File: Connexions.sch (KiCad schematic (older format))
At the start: 7 parts, among them J10 Sense2, J11 I2C, J12 Serial, J13 I2S, J7 PWM, J8 IO, J9 Sense1

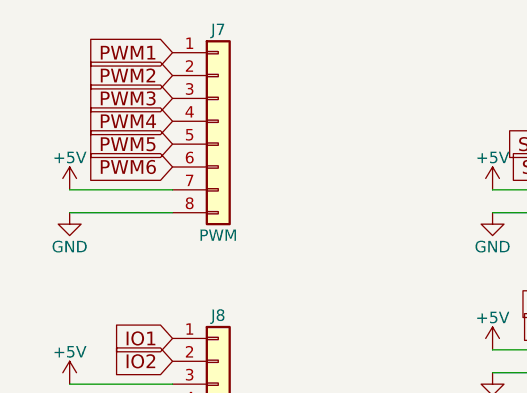
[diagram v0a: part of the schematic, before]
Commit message: Board should be ok. Bargraph leds yet to do.
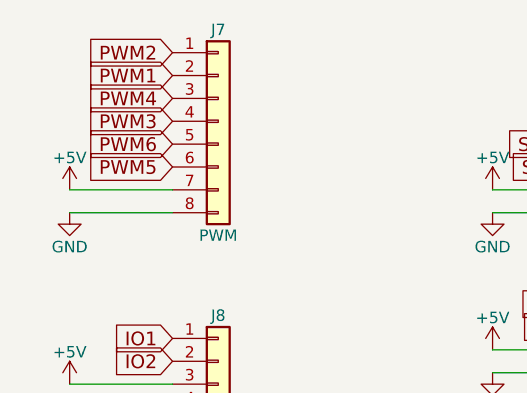
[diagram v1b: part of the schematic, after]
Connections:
- net PWM1: now also J7.2 (Pin_2); no longer J7.1 (Pin_1)
- net PWM2: now also J7.1 (Pin_1); no longer J7.2 (Pin_2)
- net PWM3: now also J7.4 (Pin_4); no longer J7.3 (Pin_3)
- net PWM4: now also J7.3 (Pin_3); no longer J7.4 (Pin_4)
- net PWM5: now also J7.6 (Pin_6); no longer J7.5 (Pin_5)
- net PWM6: now also J7.5 (Pin_5); no longer J7.6 (Pin_6)
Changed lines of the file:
@@
 Text GLabel 5700 3900 0    60   Input ~ 0
 IO2
+Text GLabel 5700 2650 0    60   Input ~ 0
+PWM1
 Text GLabel 5700 2550 0    60   Input ~ 0
-PWM1
-Text GLabel 5700 2650 0    60   Input ~ 0
 PWM2
+Text GLabel 5700 2850 0    60   Input ~ 0
+PWM3
 Text GLabel 5700 2750 0    60   Input ~ 0
-PWM3
-Text GLabel 5700 2850 0    60   Input ~ 0
 PWM4
+Text GLabel 5700 3050 0    60   Input ~ 0
+PWM5
 Text GLabel 5700 2950 0    60   Input ~ 0
-PWM5
-Text GLabel 5700 3050 0    60   Input ~ 0
 PWM6
 $Comp

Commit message: Seems to be good for fabrication launch. Probably minor things to fix.
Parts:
- renumbered J8 to J10, J9 to J11, J10 to J12, J11 to J13, J12 to J14, J13 to J15, J7 to J9
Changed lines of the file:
@@
 PWM6
 $Comp
-L Audio-Jack-2 J9
+L Audio-Jack-2 J11
 U 1 1 59B10A38
 P 5900 4500
-F 0 "J9" H 5875 4575 50  0000 C CNN
+F 0 "J11" H 5875 4575 50  0000 C CNN
 F 1 "Sense1" H 5875 4325 50  0000 C CNN
 F 2 "Connectors:PJ320D_3.5mm_Jack" H 6150 4500 50  0001 C CNN
@@
 $EndComp
 $Comp
-L GND #PWR076
+L GND #PWR080
 U 1 1 59B10AB7
 P 5600 4700
-F 0 "#PWR076" H 5600 4450 50  0001 C CNN
+F 0 "#PWR080" H 5600 4450 50  0001 C CNN
 F 1 "GND" H 5600 4550 50  0000 C CNN
 F 2 "" H 5600 4700 50  0001 C CNN
@@
 	5600 4500 5700 4500
 $Comp
-L Audio-Jack-2 J10
+L Audio-Jack-2 J12
 U 1 1 59B10F7B
 P 5900 5250
-F 0 "J10" H 5875 5325 50  0000 C CNN
+F 0 "J12" H 5875 5325 50  0000 C CNN
 F 1 "Sense2" H 5875 5075 50  0000 C CNN
 F 2 "Connectors:PJ320D_3.5mm_Jack" H 6150 5250 50  0001 C CNN
@@
 $EndComp
 $Comp
-L GND #PWR077
+L GND #PWR081
 U 1 1 59B10F81
 P 5600 5450
-F 0 "#PWR077" H 5600 5200 50  0001 C CNN
+F 0 "#PWR081" H 5600 5200 50  0001 C CNN
 F 1 "GND" H 5600 5300 50  0000 C CNN
 F 2 "" H 5600 5450 50  0001 C CNN
@@
 	5600 5250 5700 5250
 $Comp
-L Conn_01x04 J11
+L Conn_01x04 J13
 U 1 1 59B12058
 P 7650 3050
-F 0 "J11" H 7650 3250 50  0000 C CNN
+F 0 "J13" H 7650 3250 50  0000 C CNN
 F 1 "I2C" H 7650 2750 50  0000 C CNN
 F 2 "Pin_Headers:Pin_Header_Straight_1x04_Pitch2.54mm" H 7650 3050 50  0001 C CNN
@@
 I2S_MCK
 $Comp
-L Conn_01x08 J7
+L Conn_01x08 J9
 U 1 1 59B1CBF4
 P 5900 2850
-F 0 "J7" H 5900 3250 50  0000 C CNN
+F 0 "J9" H 5900 3250 50  0000 C CNN
 F 1 "PWM" H 5900 2350 50  0000 C CNN
 F 2 "Pin_Headers:Pin_Header_Straight_1x08_Pitch2.54mm" H 5900 2850 50  0001 C CNN
@@
 $EndComp
 $Comp
-L +5V #PWR078
+L +5V #PWR082
 U 1 1 59B1CCA8
 P 5250 3150
-F 0 "#PWR078" H 5250 3000 50  0001 C CNN
+F 0 "#PWR082" H 5250 3000 50  0001 C CNN
 F 1 "+5V" H 5250 3290 50  0000 C CNN
 F 2 "" H 5250 3150 50  0001 C CNN
@@
 	5250 3150 5700 3150
 $Comp
-L GND #PWR079
+L GND #PWR083
 U 1 1 59B1CCEC
 P 5250 3250
-F 0 "#PWR079" H 5250 3000 50  0001 C CNN
+F 0 "#PWR083" H 5250 3000 50  0001 C CNN
 F 1 "GND" H 5250 3100 50  0000 C CNN
 F 2 "" H 5250 3250 50  0001 C CNN
@@
 	5250 3250 5700 3250
 $Comp
-L Conn_01x04 J8
+L Conn_01x04 J10
 U 1 1 59B1CDBB
 P 5900 3900
-F 0 "J8" H 5900 4100 50  0000 C CNN
+F 0 "J10" H 5900 4100 50  0000 C CNN
 F 1 "IO" H 5900 3600 50  0000 C CNN
 F 2 "Pin_Headers:Pin_Header_Straight_1x04_Pitch2.54mm" H 5900 3900 50  0001 C CNN
@@
 $EndComp
 $Comp
-L +5V #PWR080
+L +5V #PWR084
 U 1 1 59B1CE5C
 P 5250 4000
-F 0 "#PWR080" H 5250 3850 50  0001 C CNN
+F 0 "#PWR084" H 5250 3850 50  0001 C CNN
 F 1 "+5V" H 5250 4140 50  0000 C CNN
 F 2 "" H 5250 4000 50  0001 C CNN
@@
 $EndComp
 $Comp
-L GND #PWR081
+L GND #PWR085
 U 1 1 59B1CE7C
 P 5250 4100
-F 0 "#PWR081" H 5250 3850 50  0001 C CNN
+F 0 "#PWR085" H 5250 3850 50  0001 C CNN
 F 1 "GND" H 5250 3950 50  0000 C CNN
 F 2 "" H 5250 4100 50  0001 C CNN
@@
 	5700 4000 5250 4000
 $Comp
-L Conn_01x04 J12
+L Conn_01x04 J14
 U 1 1 59B1D305
 P 7650 3750
-F 0 "J12" H 7650 3950 50  0000 C CNN
+F 0 "J14" H 7650 3950 50  0000 C CNN
 F 1 "Serial" H 7650 3450 50  0000 C CNN
 F 2 "Pin_Headers:Pin_Header_Straight_1x04_Pitch2.54mm" H 7650 3750 50  0001 C CNN
@@
 TX
 $Comp
-L +5V #PWR082
+L +5V #PWR086
 U 1 1 59B1D44B
 P 7100 3150
-F 0 "#PWR082" H 7100 3000 50  0001 C CNN
+F 0 "#PWR086" H 7100 3000 50  0001 C CNN
 F 1 "+5V" H 7100 3290 50  0000 C CNN
 F 2 "" H 7100 3150 50  0001 C CNN
@@
 $EndComp
 $Comp
-L GND #PWR083
+L GND #PWR087
 U 1 1 59B1D46E
 P 7100 3250
-F 0 "#PWR083" H 7100 3000 50  0001 C CNN
+F 0 "#PWR087" H 7100 3000 50  0001 C CNN
 F 1 "GND" H 7100 3100 50  0000 C CNN
 F 2 "" H 7100 3250 50  0001 C CNN
@@
 	7100 3250 7450 3250
 $Comp
-L +5V #PWR084
+L +5V #PWR088
 U 1 1 59B1D4D2
 P 7100 3850
-F 0 "#PWR084" H 7100 3700 50  0001 C CNN
+F 0 "#PWR088" H 7100 3700 50  0001 C CNN
 F 1 "+5V" H 7100 3990 50  0000 C CNN
 F 2 "" H 7100 3850 50  0001 C CNN
@@
 $EndComp
 $Comp
-L GND #PWR085
+L GND #PWR089
 U 1 1 59B1D4F5
 P 6750 4950
-F 0 "#PWR085" H 6750 4700 50  0001 C CNN
+F 0 "#PWR089" H 6750 4700 50  0001 C CNN
 F 1 "GND" H 6750 4800 50  0000 C CNN
 F 2 "" H 6750 4950 50  0001 C CNN
@@
 	7100 3950 7450 3950
 $Comp
-L Conn_01x06 J13
+L Conn_01x06 J15
 U 1 1 59B1D5B9
 P 7650 4650
-F 0 "J13" H 7650 4950 50  0000 C CNN
+F 0 "J15" H 7650 4950 50  0000 C CNN
 F 1 "I2S" H 7650 4250 50  0000 C CNN
 F 2 "Pin_Headers:Pin_Header_Straight_1x06_Pitch2.54mm" H 7650 4650 50  0001 C CNN
@@
 $EndComp
 $Comp
-L +3.3V #PWR086
+L +3.3V #PWR090
 U 1 1 59B1D6B1
 P 6750 4850
-F 0 "#PWR086" H 6750 4700 50  0001 C CNN
+F 0 "#PWR090" H 6750 4700 50  0001 C CNN
 F 1 "+3.3V" H 6750 4990 50  0000 C CNN
 F 2 "" H 6750 4850 50  0001 C CNN
@@
 	6750 4950 7450 4950
 $Comp
-L GND #PWR087
+L GND #PWR091
 U 1 1 59C9F2EB
 P 7100 3950
-F 0 "#PWR087" H 7100 3700 50  0001 C CNN
+F 0 "#PWR091" H 7100 3700 50  0001 C CNN
 F 1 "GND" H 7100 3800 50  0000 C CNN
 F 2 "" H 7100 3950 50  0001 C CNN

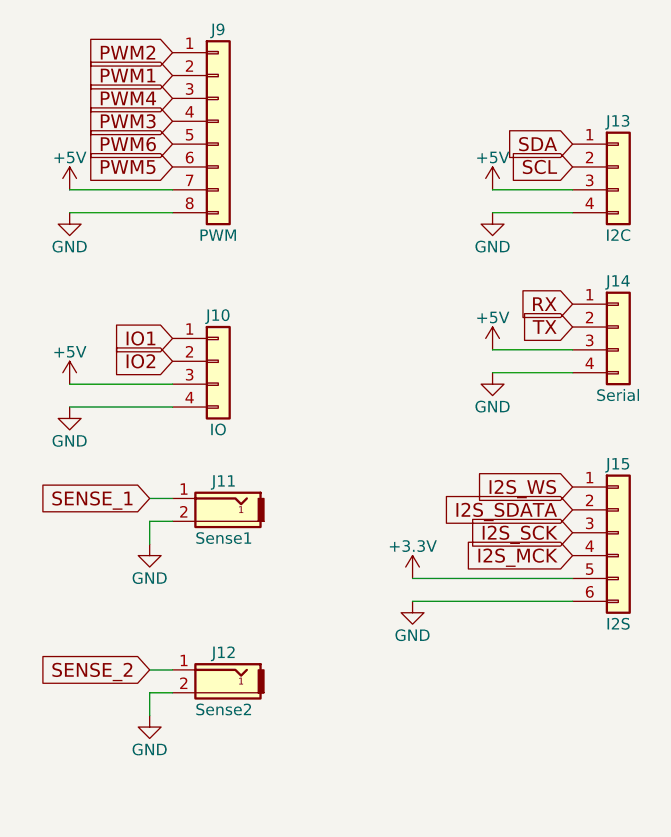
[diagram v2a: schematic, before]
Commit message: Board modified after ckecking. Ready for fab, just need to create gerber, position and components files.
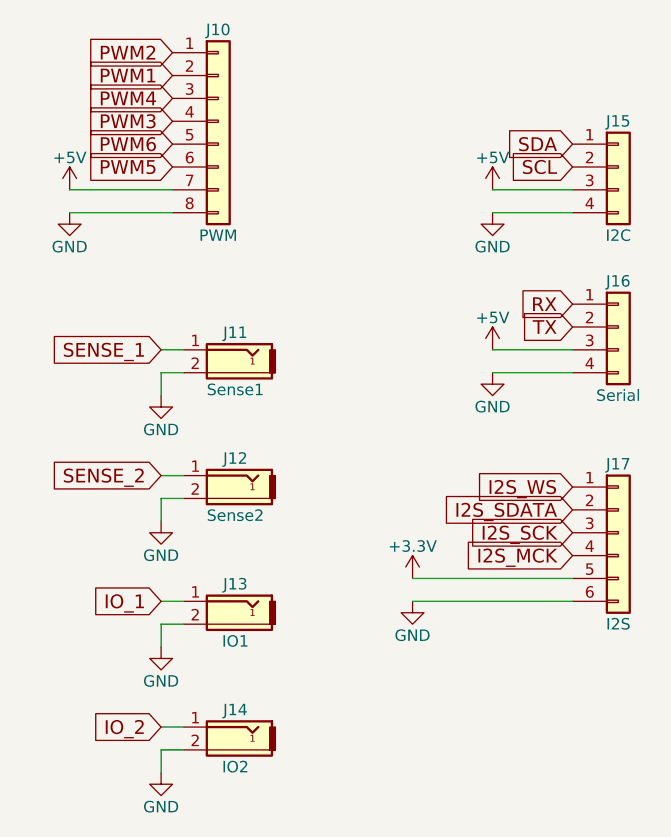
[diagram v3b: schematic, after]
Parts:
- removed J10: IO, Pin_Headers:Pin_Header_Straight_1x04_Pitch2.54mm, symbol Conn_01x04
- added J13: IO1, Connectors:PJ320D_3.5mm_Jack, symbol Audio-Jack-2
- added J14: IO2, Connectors:PJ320D_3.5mm_Jack, symbol Audio-Jack-2
- renumbered J9 to J10, J13 to J15, J14 to J16, J15 to J17
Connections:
- net GND: now also J13.2, J14.2
- new net IO_1: J13.1
- new net IO_2: J14.1
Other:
- moved on the sheet: J11, J12
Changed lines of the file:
@@
 EESchema Schematic File Version 2
+LIBS:ContactConsequencesMono-rescue
 LIBS:switches-perso
 LIBS:Logos
@@
 Comment4 ""
 $EndDescr
-Text GLabel 5700 3800 0    60   Input ~ 0
-IO1
-Text GLabel 5700 3900 0    60   Input ~ 0
-IO2
 Text GLabel 5700 2650 0    60   Input ~ 0
 PWM1
@@
 L Audio-Jack-2 J11
 U 1 1 59B10A38
-P 5900 4500
-F 0 "J11" H 5875 4575 50  0000 C CNN
-F 1 "Sense1" H 5875 4325 50  0000 C CNN
-F 2 "Connectors:PJ320D_3.5mm_Jack" H 6150 4500 50  0001 C CNN
-F 3 "" H 6150 4500 50  0001 C CNN
-	1    5900 4500
+P 5950 3850
+F 0 "J11" H 5925 3925 50  0000 C CNN
+F 1 "Sense1" H 5925 3675 50  0000 C CNN
+F 2 "Connectors:PJ320D_3.5mm_Jack" H 6200 3850 50  0001 C CNN
+F 3 "" H 6200 3850 50  0001 C CNN
+	1    5950 3850
 	-1   0    0    -1
 $EndComp
 $Comp
-L GND #PWR080
+L GND #PWR088
 U 1 1 59B10AB7
-P 5600 4700
-F 0 "#PWR080" H 5600 4450 50  0001 C CNN
-F 1 "GND" H 5600 4550 50  0000 C CNN
-F 2 "" H 5600 4700 50  0001 C CNN
-F 3 "" H 5600 4700 50  0001 C CNN
-	1    5600 4700
-	1    0    0    -1
-$EndComp
-Wire Wire Line
-	5600 4700 5600 4600
-Wire Wire Line
-	5600 4600 5700 4600
-Text GLabel 5600 4500 0    60   Input ~ 0
+P 5650 4050
+F 0 "#PWR088" H 5650 3800 50  0001 C CNN
+F 1 "GND" H 5650 3900 50  0000 C CNN
+F 2 "" H 5650 4050 50  0001 C CNN
+F 3 "" H 5650 4050 50  0001 C CNN
+	1    5650 4050
+	1    0    0    -1
+$EndComp
+Wire Wire Line
+	5650 4050 5650 3950
+Wire Wire Line
+	5650 3950 5750 3950
+Text GLabel 5650 3850 0    60   Input ~ 0
 SENSE_1
 Wire Wire Line
-	5600 4500 5700 4500
+	5650 3850 5750 3850
 $Comp
 L Audio-Jack-2 J12
 U 1 1 59B10F7B
-P 5900 5250
-F 0 "J12" H 5875 5325 50  0000 C CNN
-F 1 "Sense2" H 5875 5075 50  0000 C CNN
-F 2 "Connectors:PJ320D_3.5mm_Jack" H 6150 5250 50  0001 C CNN
-F 3 "" H 6150 5250 50  0001 C CNN
-	1    5900 5250
+P 5950 4400
+F 0 "J12" H 5925 4475 50  0000 C CNN
+F 1 "Sense2" H 5925 4225 50  0000 C CNN
+F 2 "Connectors:PJ320D_3.5mm_Jack" H 6200 4400 50  0001 C CNN
+F 3 "" H 6200 4400 50  0001 C CNN
+	1    5950 4400
 	-1   0    0    -1
 $EndComp
 $Comp
-L GND #PWR081
+L GND #PWR089
 U 1 1 59B10F81
-P 5600 5450
-F 0 "#PWR081" H 5600 5200 50  0001 C CNN
-F 1 "GND" H 5600 5300 50  0000 C CNN
-F 2 "" H 5600 5450 50  0001 C CNN
-F 3 "" H 5600 5450 50  0001 C CNN
-	1    5600 5450
-	1    0    0    -1
-$EndComp
-Wire Wire Line
-	5600 5450 5600 5350
-Wire Wire Line
-	5600 5350 5700 5350
-Text GLabel 5600 5250 0    60   Input ~ 0
+P 5650 4600
+F 0 "#PWR089" H 5650 4350 50  0001 C CNN
+F 1 "GND" H 5650 4450 50  0000 C CNN
+F 2 "" H 5650 4600 50  0001 C CNN
+F 3 "" H 5650 4600 50  0001 C CNN
+	1    5650 4600
+	1    0    0    -1
+$EndComp
+Wire Wire Line
+	5650 4600 5650 4500
+Wire Wire Line
+	5650 4500 5750 4500
+Text GLabel 5650 4400 0    60   Input ~ 0
 SENSE_2
 Wire Wire Line
-	5600 5250 5700 5250
-$Comp
-L Conn_01x04 J13
+	5650 4400 5750 4400
+$Comp
+L Conn_01x04 J15
 U 1 1 59B12058
 P 7650 3050
-F 0 "J13" H 7650 3250 50  0000 C CNN
+F 0 "J15" H 7650 3250 50  0000 C CNN
 F 1 "I2C" H 7650 2750 50  0000 C CNN
 F 2 "Pin_Headers:Pin_Header_Straight_1x04_Pitch2.54mm" H 7650 3050 50  0001 C CNN
@@
 I2S_MCK
 $Comp
-L Conn_01x08 J9
+L Conn_01x08 J10
 U 1 1 59B1CBF4
 P 5900 2850
-F 0 "J9" H 5900 3250 50  0000 C CNN
+F 0 "J10" H 5900 3250 50  0000 C CNN
 F 1 "PWM" H 5900 2350 50  0000 C CNN
 F 2 "Pin_Headers:Pin_Header_Straight_1x08_Pitch2.54mm" H 5900 2850 50  0001 C CNN
@@
 $EndComp
 $Comp
-L +5V #PWR082
+L +5V #PWR090
 U 1 1 59B1CCA8
 P 5250 3150
-F 0 "#PWR082" H 5250 3000 50  0001 C CNN
+F 0 "#PWR090" H 5250 3000 50  0001 C CNN
 F 1 "+5V" H 5250 3290 50  0000 C CNN
 F 2 "" H 5250 3150 50  0001 C CNN
@@
 	5250 3150 5700 3150
 $Comp
-L GND #PWR083
+L GND #PWR091
 U 1 1 59B1CCEC
 P 5250 3250
-F 0 "#PWR083" H 5250 3000 50  0001 C CNN
+F 0 "#PWR091" H 5250 3000 50  0001 C CNN
 F 1 "GND" H 5250 3100 50  0000 C CNN
 F 2 "" H 5250 3250 50  0001 C CNN
@@
 	5250 3250 5700 3250
 $Comp
-L Conn_01x04 J10
-U 1 1 59B1CDBB
-P 5900 3900
-F 0 "J10" H 5900 4100 50  0000 C CNN
-F 1 "IO" H 5900 3600 50  0000 C CNN
-F 2 "Pin_Headers:Pin_Header_Straight_1x04_Pitch2.54mm" H 5900 3900 50  0001 C CNN
-F 3 "" H 5900 3900 50  0001 C CNN
-	1    5900 3900
-	1    0    0    -1
-$EndComp
-$Comp
-L +5V #PWR084
-U 1 1 59B1CE5C
-P 5250 4000
-F 0 "#PWR084" H 5250 3850 50  0001 C CNN
-F 1 "+5V" H 5250 4140 50  0000 C CNN
-F 2 "" H 5250 4000 50  0001 C CNN
-F 3 "" H 5250 4000 50  0001 C CNN
-	1    5250 4000
-	1    0    0    -1
-$EndComp
-$Comp
-L GND #PWR085
-U 1 1 59B1CE7C
-P 5250 4100
-F 0 "#PWR085" H 5250 3850 50  0001 C CNN
-F 1 "GND" H 5250 3950 50  0000 C CNN
-F 2 "" H 5250 4100 50  0001 C CNN
-F 3 "" H 5250 4100 50  0001 C CNN
-	1    5250 4100
-	1    0    0    -1
-$EndComp
-Wire Wire Line
-	5250 4100 5700 4100
-Wire Wire Line
-	5700 4000 5250 4000
-$Comp
-L Conn_01x04 J14
+L Conn_01x04 J16
 U 1 1 59B1D305
 P 7650 3750
-F 0 "J14" H 7650 3950 50  0000 C CNN
+F 0 "J16" H 7650 3950 50  0000 C CNN
 F 1 "Serial" H 7650 3450 50  0000 C CNN
 F 2 "Pin_Headers:Pin_Header_Straight_1x04_Pitch2.54mm" H 7650 3750 50  0001 C CNN
@@
 TX
 $Comp
-L +5V #PWR086
+L +5V #PWR092
 U 1 1 59B1D44B
 P 7100 3150
-F 0 "#PWR086" H 7100 3000 50  0001 C CNN
+F 0 "#PWR092" H 7100 3000 50  0001 C CNN
 F 1 "+5V" H 7100 3290 50  0000 C CNN
 F 2 "" H 7100 3150 50  0001 C CNN
@@
 $EndComp
 $Comp
-L GND #PWR087
+L GND #PWR093
 U 1 1 59B1D46E
 P 7100 3250
-F 0 "#PWR087" H 7100 3000 50  0001 C CNN
+F 0 "#PWR093" H 7100 3000 50  0001 C CNN
 F 1 "GND" H 7100 3100 50  0000 C CNN
 F 2 "" H 7100 3250 50  0001 C CNN
@@
 	7100 3250 7450 3250
 $Comp
-L +5V #PWR088
+L +5V #PWR094
 U 1 1 59B1D4D2
 P 7100 3850
-F 0 "#PWR088" H 7100 3700 50  0001 C CNN
+F 0 "#PWR094" H 7100 3700 50  0001 C CNN
 F 1 "+5V" H 7100 3990 50  0000 C CNN
 F 2 "" H 7100 3850 50  0001 C CNN
@@
 $EndComp
 $Comp
-L GND #PWR089
+L GND #PWR095
 U 1 1 59B1D4F5
 P 6750 4950
-F 0 "#PWR089" H 6750 4700 50  0001 C CNN
+F 0 "#PWR095" H 6750 4700 50  0001 C CNN
 F 1 "GND" H 6750 4800 50  0000 C CNN
 F 2 "" H 6750 4950 50  0001 C CNN
@@
 	7100 3950 7450 3950
 $Comp
-L Conn_01x06 J15
+L Conn_01x06 J17
 U 1 1 59B1D5B9
 P 7650 4650
-F 0 "J15" H 7650 4950 50  0000 C CNN
+F 0 "J17" H 7650 4950 50  0000 C CNN
 F 1 "I2S" H 7650 4250 50  0000 C CNN
 F 2 "Pin_Headers:Pin_Header_Straight_1x06_Pitch2.54mm" H 7650 4650 50  0001 C CNN
@@
 $EndComp
 $Comp
-L +3.3V #PWR090
+L +3.3V #PWR096
 U 1 1 59B1D6B1
 P 6750 4850
-F 0 "#PWR090" H 6750 4700 50  0001 C CNN
+F 0 "#PWR096" H 6750 4700 50  0001 C CNN
 F 1 "+3.3V" H 6750 4990 50  0000 C CNN
 F 2 "" H 6750 4850 50  0001 C CNN
@@
 	6750 4950 7450 4950
 $Comp
-L GND #PWR091
+L GND #PWR097
 U 1 1 59C9F2EB
 P 7100 3950
-F 0 "#PWR091" H 7100 3700 50  0001 C CNN
+F 0 "#PWR097" H 7100 3700 50  0001 C CNN
 F 1 "GND" H 7100 3800 50  0000 C CNN
 F 2 "" H 7100 3950 50  0001 C CNN
@@
 	1    0    0    -1
 $EndComp
+$Comp
+L Audio-Jack-2 J13
+U 1 1 59F9AE4A
+P 5950 4950
+F 0 "J13" H 5925 5025 50  0000 C CNN
+F 1 "IO1" H 5925 4775 50  0000 C CNN
+F 2 "Connectors:PJ320D_3.5mm_Jack" H 6200 4950 50  0001 C CNN
+F 3 "" H 6200 4950 50  0001 C CNN
+	1    5950 4950
+	-1   0    0    -1
+$EndComp
+$Comp
+L GND #PWR098
+U 1 1 59F9AE50
+P 5650 5150
+F 0 "#PWR098" H 5650 4900 50  0001 C CNN
+F 1 "GND" H 5650 5000 50  0000 C CNN
+F 2 "" H 5650 5150 50  0001 C CNN
+F 3 "" H 5650 5150 50  0001 C CNN
+	1    5650 5150
+	1    0    0    -1
+$EndComp
+Wire Wire Line
+	5650 5150 5650 5050
+Wire Wire Line
+	5650 5050 5750 5050
+Text GLabel 5650 4950 0    60   Input ~ 0
+IO_1
+Wire Wire Line
+	5650 4950 5750 4950
+$Comp
+L Audio-Jack-2 J14
+U 1 1 59F9AFC6
+P 5950 5500
+F 0 "J14" H 5925 5575 50  0000 C CNN
+F 1 "IO2" H 5925 5325 50  0000 C CNN
+F 2 "Connectors:PJ320D_3.5mm_Jack" H 6200 5500 50  0001 C CNN
+F 3 "" H 6200 5500 50  0001 C CNN
+	1    5950 5500
+	-1   0    0    -1
+$EndComp
+$Comp
+L GND #PWR099
+U 1 1 59F9AFCC
+P 5650 5700
+F 0 "#PWR099" H 5650 5450 50  0001 C CNN
+F 1 "GND" H 5650 5550 50  0000 C CNN
+F 2 "" H 5650 5700 50  0001 C CNN
+F 3 "" H 5650 5700 50  0001 C CNN
+	1    5650 5700
+	1    0    0    -1
+$EndComp
+Wire Wire Line
+	5650 5700 5650 5600
+Wire Wire Line
+	5650 5600 5750 5600
+Text GLabel 5650 5500 0    60   Input ~ 0
+IO_2
+Wire Wire Line
+	5650 5500 5750 5500
 $EndSCHEMATC

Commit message: v0.2 ready for fabrication. Voltage regulators replaced by cheaper ones.
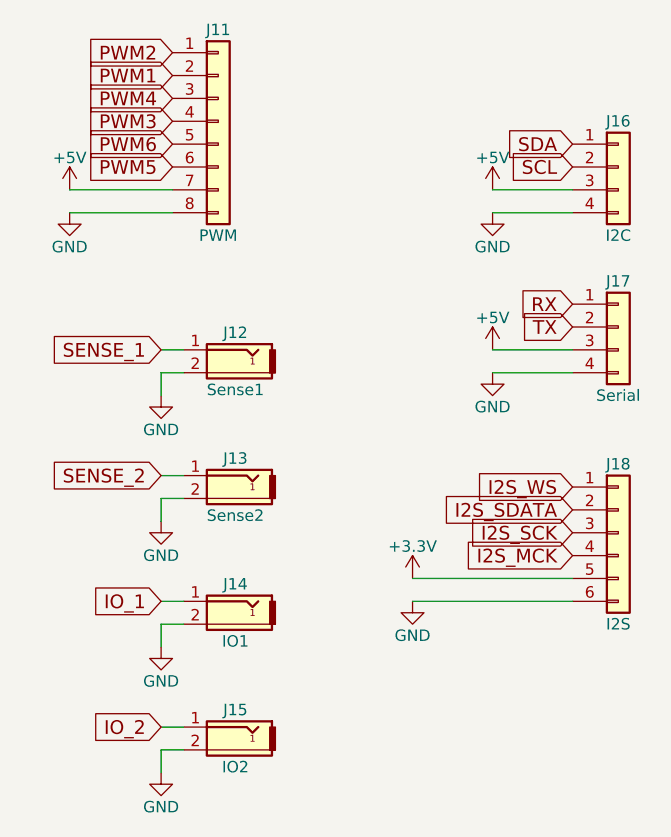
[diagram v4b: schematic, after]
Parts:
- renumbered J10 to J11, J11 to J12, J12 to J13, J13 to J14, J14 to J15, J15 to J16, J16 to J17, J17 to J18
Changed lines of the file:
@@
 PWM6
 $Comp
-L Audio-Jack-2 J11
+L Audio-Jack-2 J12
 U 1 1 59B10A38
 P 5950 3850
-F 0 "J11" H 5925 3925 50  0000 C CNN
+F 0 "J12" H 5925 3925 50  0000 C CNN
 F 1 "Sense1" H 5925 3675 50  0000 C CNN
 F 2 "Connectors:PJ320D_3.5mm_Jack" H 6200 3850 50  0001 C CNN
@@
 	5650 3850 5750 3850
 $Comp
-L Audio-Jack-2 J12
+L Audio-Jack-2 J13
 U 1 1 59B10F7B
 P 5950 4400
-F 0 "J12" H 5925 4475 50  0000 C CNN
+F 0 "J13" H 5925 4475 50  0000 C CNN
 F 1 "Sense2" H 5925 4225 50  0000 C CNN
 F 2 "Connectors:PJ320D_3.5mm_Jack" H 6200 4400 50  0001 C CNN
@@
 	5650 4400 5750 4400
 $Comp
-L Conn_01x04 J15
+L Conn_01x04 J16
 U 1 1 59B12058
 P 7650 3050
-F 0 "J15" H 7650 3250 50  0000 C CNN
+F 0 "J16" H 7650 3250 50  0000 C CNN
 F 1 "I2C" H 7650 2750 50  0000 C CNN
 F 2 "Pin_Headers:Pin_Header_Straight_1x04_Pitch2.54mm" H 7650 3050 50  0001 C CNN
@@
 I2S_MCK
 $Comp
-L Conn_01x08 J10
+L Conn_01x08 J11
 U 1 1 59B1CBF4
 P 5900 2850
-F 0 "J10" H 5900 3250 50  0000 C CNN
+F 0 "J11" H 5900 3250 50  0000 C CNN
 F 1 "PWM" H 5900 2350 50  0000 C CNN
 F 2 "Pin_Headers:Pin_Header_Straight_1x08_Pitch2.54mm" H 5900 2850 50  0001 C CNN
@@
 	5250 3250 5700 3250
 $Comp
-L Conn_01x04 J16
+L Conn_01x04 J17
 U 1 1 59B1D305
 P 7650 3750
-F 0 "J16" H 7650 3950 50  0000 C CNN
+F 0 "J17" H 7650 3950 50  0000 C CNN
 F 1 "Serial" H 7650 3450 50  0000 C CNN
 F 2 "Pin_Headers:Pin_Header_Straight_1x04_Pitch2.54mm" H 7650 3750 50  0001 C CNN
@@
 	7100 3950 7450 3950
 $Comp
-L Conn_01x06 J17
+L Conn_01x06 J18
 U 1 1 59B1D5B9
 P 7650 4650
-F 0 "J17" H 7650 4950 50  0000 C CNN
+F 0 "J18" H 7650 4950 50  0000 C CNN
 F 1 "I2S" H 7650 4250 50  0000 C CNN
 F 2 "Pin_Headers:Pin_Header_Straight_1x06_Pitch2.54mm" H 7650 4650 50  0001 C CNN
@@
 $EndComp
 $Comp
-L Audio-Jack-2 J13
+L Audio-Jack-2 J14
 U 1 1 59F9AE4A
 P 5950 4950
-F 0 "J13" H 5925 5025 50  0000 C CNN
+F 0 "J14" H 5925 5025 50  0000 C CNN
 F 1 "IO1" H 5925 4775 50  0000 C CNN
 F 2 "Connectors:PJ320D_3.5mm_Jack" H 6200 4950 50  0001 C CNN
@@
 	5650 4950 5750 4950
 $Comp
-L Audio-Jack-2 J14
+L Audio-Jack-2 J15
 U 1 1 59F9AFC6
 P 5950 5500
-F 0 "J14" H 5925 5575 50  0000 C CNN
+F 0 "J15" H 5925 5575 50  0000 C CNN
 F 1 "IO2" H 5925 5325 50  0000 C CNN
 F 2 "Connectors:PJ320D_3.5mm_Jack" H 6200 5500 50  0001 C CNN
